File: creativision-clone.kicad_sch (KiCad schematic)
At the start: 102 parts, among them J1 Conn_01x10_Socket, J2 Conn_01x10_Socket, J3 Conn_01x07_Pin, J4 Conn_01x04_Socket, J5 RCJ-013, J6 RCJ-014, P1 Cartridge Slot, Q1 2n4401, SW1 Reset, SW2 SW_DPDT_x2, U1 AS6C62256-DIP, U100 74HCT574, U101 74HCT574, U102 74HCT574, U12 74LS32, U15 74LS139, U18 AS6C62256-DIP, U2 6502, U20 27256, U21 6821, U22 SN76489AN, U3 TMS9918A, U99 74HCT04, X1 2MHz, X2 USB-B1HSB6, Y1 10.73863MHz

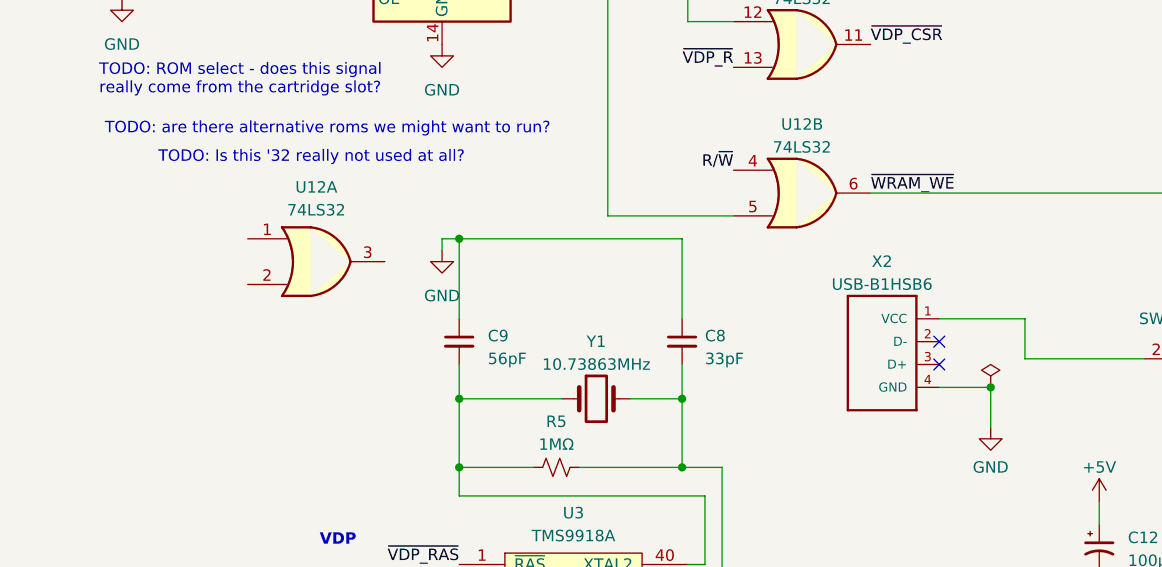
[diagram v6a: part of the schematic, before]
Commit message: Beginning footprint assignment
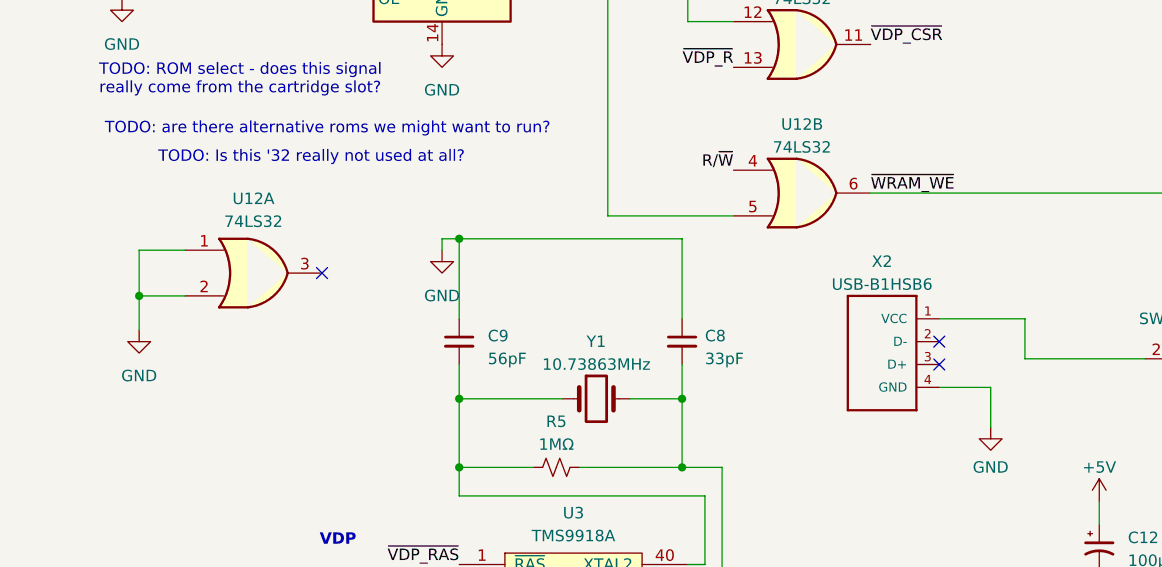
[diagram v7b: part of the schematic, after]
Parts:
- J5: footprint CUI_RCJ-017 -> Jacks:CUI_RCJ-017;  Manufacturer recommendations -> (none); Digi-Key (none) -> Manufacturer recommendations
- J6: footprint CUI_RCJ-017 -> Jacks:CUI_RCJ-017;  Manufacturer recommendations -> (none)
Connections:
- net GND: now also U12.1, U12.2
- no-connect marks 11 -> 12
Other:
- moved on the sheet: U12A
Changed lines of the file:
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@@
   (junction (at 307.975 66.675) (diameter 0) (color 0 0 0 0)
   )
+  (junction (at 18.415 204.47) (diameter 0) (color 0 0 0 0)
+  )
   (junction (at 328.93 22.86) (diameter 0) (color 0 0 0 0)
   )
@@
   (junction (at 310.515 73.025) (diameter 0) (color 0 0 0 0)
   )
-  (junction (at 113.03 214.63) (diameter 0) (color 0 0 0 0)
-  )
   (junction (at 325.755 165.735) (diameter 0) (color 0 0 0 0)
   )
@@
   (no_connect (at 79.375 239.395))
   (no_connect (at 107.315 212.09))
+  (no_connect (at 38.735 201.93))
   (no_connect (at 82.55 116.84))
   (no_connect (at 82.55 129.54))
@@
     (stroke (width 0) (type default))
   )
+  (wire (pts (xy 18.415 204.47) (xy 23.495 204.47))
+    (stroke (width 0) (type default))
+  )
   (wire (pts (xy 331.47 52.705) (xy 331.47 69.215))
     (stroke (width 0) (type default))
@@
     (stroke (width 0) (type default))
   )
+  (wire (pts (xy 18.415 199.39) (xy 23.495 199.39))
+    (stroke (width 0) (type default))
+  )
   (wire (pts (xy 319.405 88.265) (xy 302.895 88.265))
     (stroke (width 0) (type default))
@@
     (stroke (width 0) (type default))
   )
+  (wire (pts (xy 18.415 208.28) (xy 18.415 204.47))
+    (stroke (width 0) (type default))
+  )
   (wire (pts (xy 276.86 233.045) (xy 276.86 229.235))
     (stroke (width 0) (type default))
@@
     (stroke (width 0) (type default))
   )
+  (wire (pts (xy 18.415 204.47) (xy 18.415 199.39))
+    (stroke (width 0) (type default))
+  )
   (wire (pts (xy 129.54 57.15) (xy 141.605 57.15))
     (stroke (width 0) (type default))
@@
     )
   )
-  (symbol (lib_id "power:PWR_FLAG") (at 113.03 214.63 0) (unit 1)
-    (in_bom yes) (on_board yes) (dnp no) (fields_autoplaced)
-    (property "Reference" "#FLG05" (at 113.03 212.725 0)
-      (effects (font (size 1.27 1.27)) hide)
-    )
-    (property "Value" "PWR_FLAG" (at 113.03 210.82 0)
-      (effects (font (size 1.27 1.27)) hide)
-    )
-    (property "Footprint" "" (at 113.03 214.63 0)
-      (effects (font (size 1.27 1.27)) hide)
-    )
-    (property "Datasheet" "~" (at 113.03 214.63 0)
-      (effects (font (size 1.27 1.27)) hide)
-    )
-    (pin "1")
-    (instances
-      (project "creativision-clone"
-        (path "/4f154aad-bddd-4366-bec7-a527fffe24b1"
-          (reference "#FLG05") (unit 1)
-        )
-      )
-    )
-  )
   (symbol (lib_id "power:+9V") (at 153.67 233.68 0) (unit 1)
     (in_bom yes) (on_board yes) (dnp no) (fields_autoplaced)
@@
     )
   )
+  (symbol (lib_id "power:GND") (at 18.415 208.28 0) (unit 1)
+    (in_bom yes) (on_board yes) (dnp no) (fields_autoplaced)
+    (property "Reference" "#PWR070" (at 18.415 214.63 0)
+      (effects (font (size 1.27 1.27)) hide)
+    )
+    (property "Value" "GND" (at 18.415 213.36 0)
+      (effects (font (size 1.27 1.27)))
+    )
+    (property "Footprint" "" (at 18.415 208.28 0)
+      (effects (font (size 1.27 1.27)) hide)
+    )
+    (property "Datasheet" "" (at 18.415 208.28 0)
+      (effects (font (size 1.27 1.27)) hide)
+    )
+    (pin "1")
+    (instances
+      (project "creativision-clone"
+        (path "/4f154aad-bddd-4366-bec7-a527fffe24b1"
+          (reference "#PWR070") (unit 1)
+        )
+      )
+    )
+  )
   (symbol (lib_id "power:GND") (at 158.75 299.085 0) (unit 1)
     (in_bom yes) (on_board yes) (dnp no) (fields_autoplaced)
@@
       (effects (font (size 1.27 1.27)) (justify right))
     )
-    (property "Footprint" "CUI_RCJ-017" (at 383.54 187.325 0)
+    (property "Footprint" "Jacks:CUI_RCJ-017" (at 383.54 187.325 0)
       (effects (font (size 1.27 1.27)) (justify left bottom) hide)
     )
@@
       (effects (font (size 1.27 1.27)) (justify left bottom) hide)
     )
-    (property "" "Manufacturer recommendations" (at 383.54 187.325 0)
+    (property "Digi-Key" "Manufacturer recommendations" (at 383.54 187.325 0)
       (effects (font (size 1.27 1.27)) (justify left bottom) hide)
     )
@@
       (effects (font (size 1.27 1.27)))
     )
-    (property "Footprint" "CUI_RCJ-017" (at 383.54 168.275 0)
+    (property "Footprint" "Jacks:CUI_RCJ-017" (at 383.54 168.275 0)
       (effects (font (size 1.27 1.27)) (justify left bottom) hide)
     )
@@
       (effects (font (size 1.27 1.27)) (justify left bottom) hide)
     )
-    (property "" "Manufacturer recommendations" (at 383.54 168.275 0)
+    (property "Digi-Key" "" (at 383.54 168.275 0)
       (effects (font (size 1.27 1.27)) (justify left bottom) hide)
     )
+    (property "Field5" "" (at 383.54 168.275 0)
+      (effects (font (size 1.27 1.27)) hide)
+    )
     (pin "1A")
     (pin "1B")
@@
     )
   )
-  (symbol (lib_id "74xx:74LS32") (at 38.1 200.66 0) (unit 1)
+  (symbol (lib_id "74xx:74LS32") (at 31.115 201.93 0) (unit 1)
     (in_bom yes) (on_board yes) (dnp no) (fields_autoplaced)
-    (property "Reference" "U12" (at 38.1 192.405 0)
+    (property "Reference" "U12" (at 31.115 193.675 0)
       (effects (font (size 1.27 1.27)))
     )
-    (property "Value" "74LS32" (at 38.1 194.945 0)
+    (property "Value" "74LS32" (at 31.115 196.215 0)
       (effects (font (size 1.27 1.27)))
     )
-    (property "Footprint" "" (at 38.1 200.66 0)
+    (property "Footprint" "" (at 31.115 201.93 0)
       (effects (font (size 1.27 1.27)) hide)
     )
-    (property "Datasheet" "http://www.ti.com/lit/gpn/sn74LS32" (at 38.1 200.66 0)
+    (property "Datasheet" "http://www.ti.com/lit/gpn/sn74LS32" (at 31.115 201.93 0)
       (effects (font (size 1.27 1.27)) hide)
     )

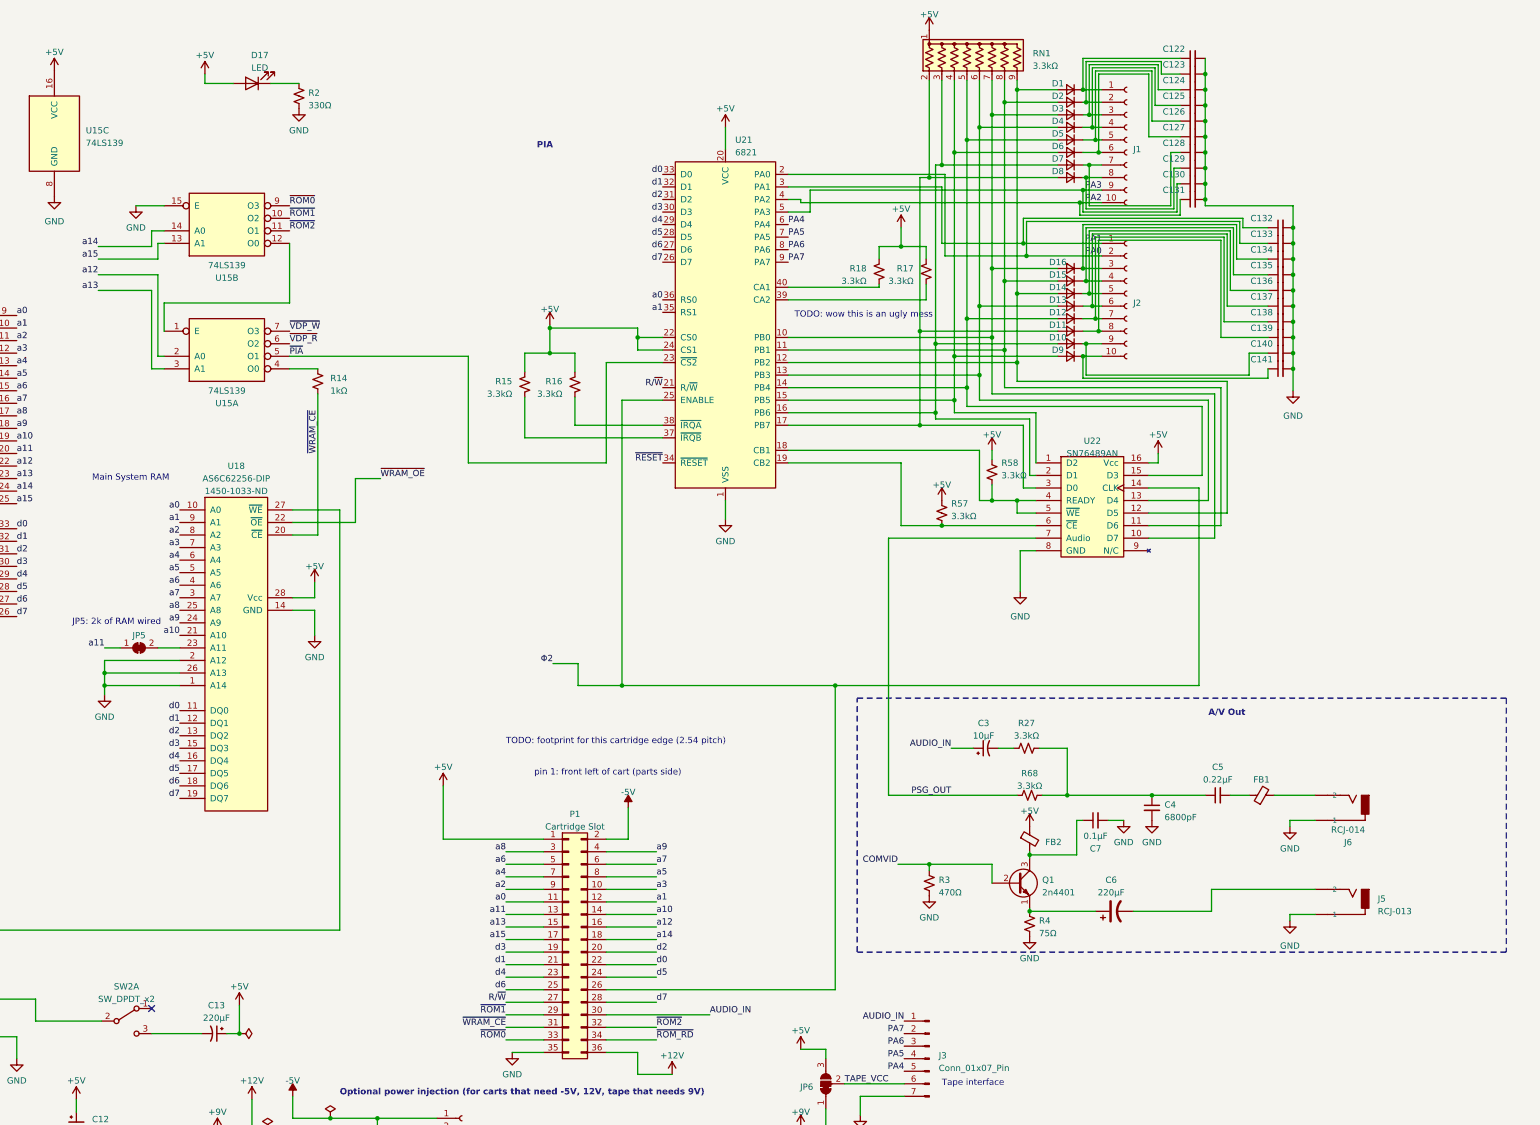
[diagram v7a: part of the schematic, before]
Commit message: Almost complete footprint assignment
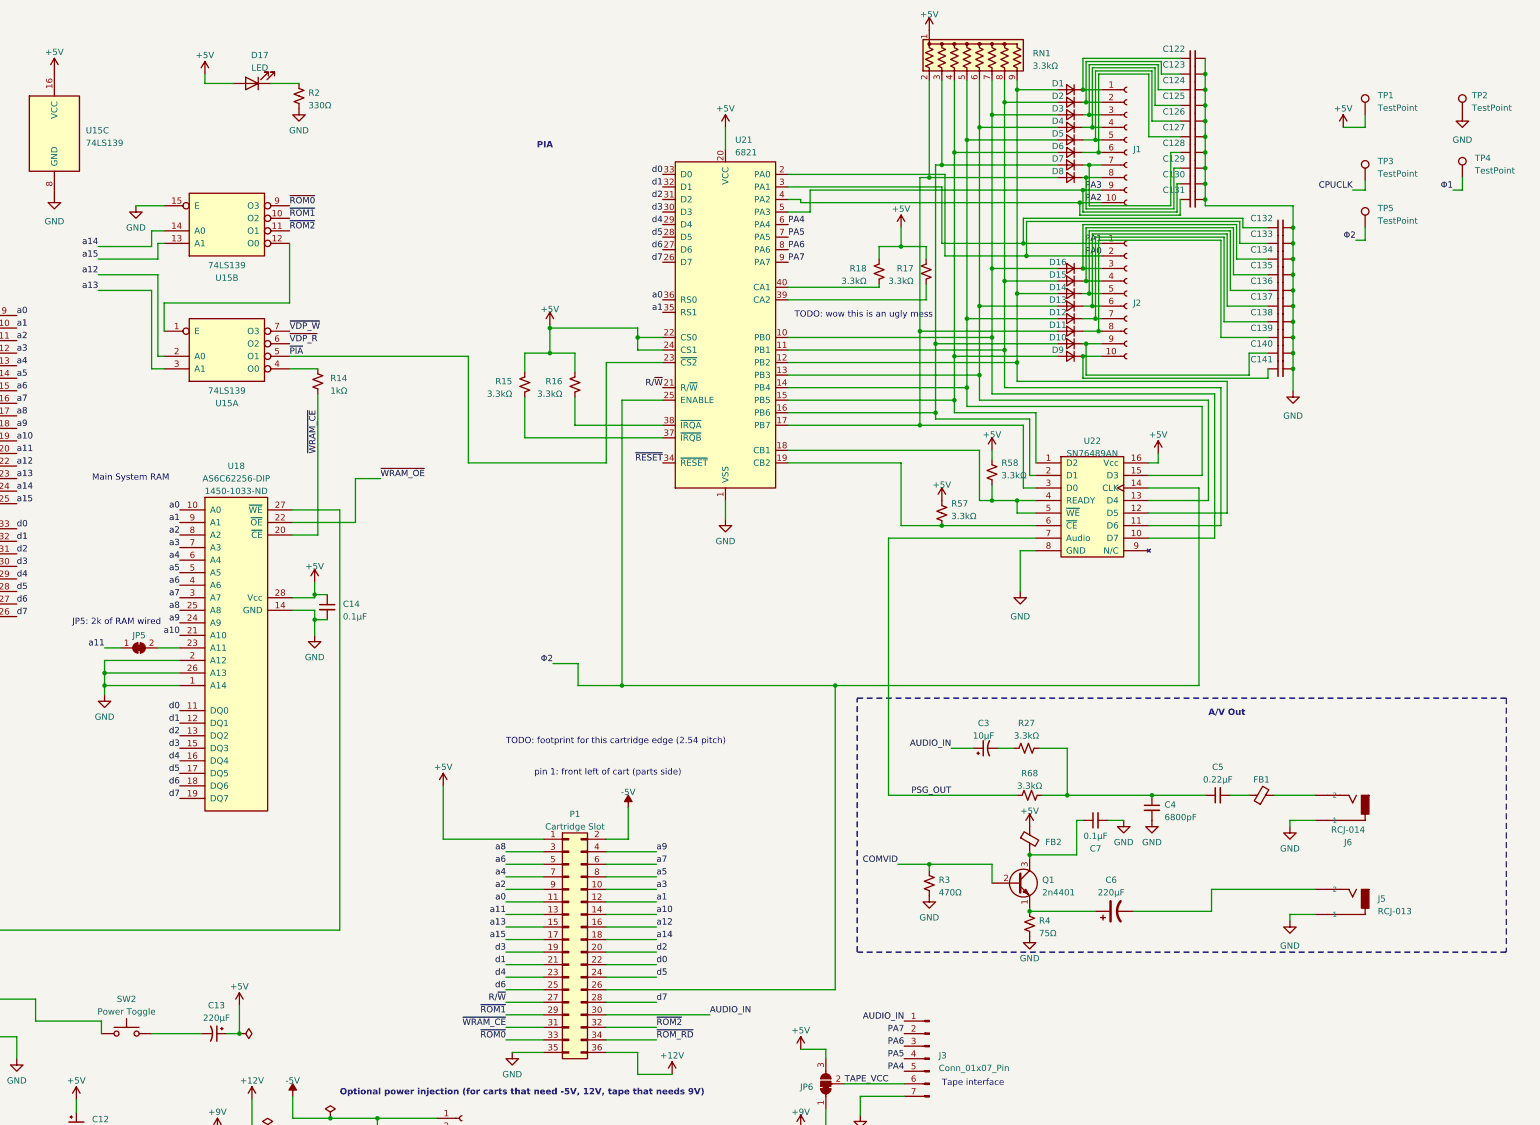
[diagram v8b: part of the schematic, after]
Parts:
- removed SW2: SW_DPDT_x2, symbol Switch:SW_DPDT_x2
- added C14: 0.1µF, Capacitor_THT:C_Disc_D5.0mm_W2.5mm_P2.50mm, symbol Device:C_Small
- added SW2: Power Toggle, LeakyChips:PVA1_Switch, symbol Switch:SW_Push
- added TP1, TP2, TP3, TP4, TP5: TestPoint, TestPoint:TestPoint_Loop_D2.50mm_Drill1.0mm, symbol Connector:TestPoint
- C1, C122, C123, C124, C125, C126, C127, C128, C129, C130, C131, C132, C133, C134, C135, C136, C137, C138, C139, C140, C141, C2, C4, C5, C7, C8, C9: footprint (none) -> Capacitor_THT:C_Disc_D5.0mm_W2.5mm_P2.50mm
- C10, C106, C11, C12, C13, C6: footprint (none) -> Capacitor_THT:CP_Radial_D6.3mm_P2.50mm
- C3: footprint (none) -> Capacitor_THT:CP_Radial_D5.0mm_P2.50mm
- D1, D10, D11, D12, D13, D14, D15, D16, D2, D3, D4, D5, D6, D7, D8, D9: footprint (none) -> Diode_THT:D_DO-35_SOD27_P7.62mm_Horizontal
- D17: footprint (none) -> LED_THT:LED_D3.0mm
- FB1, FB2: footprint (none) -> Resistor_THT:R_Axial_DIN0309_L9.0mm_D3.2mm_P12.70mm_Horizontal; DigiKey (none) -> 1934-1476-2-ND
- J1, J2: footprint (none) -> Connector_PinSocket_2.54mm:PinSocket_1x10_P2.54mm_Vertical
- J3: footprint (none) -> Connector_PinHeader_2.54mm:PinHeader_1x07_P2.54mm_Horizontal
- J4: footprint (none) -> Connector_PinSocket_2.54mm:PinSocket_1x04_P2.54mm_Vertical
- JP1, JP2, JP3, JP4, JP5: footprint (none) -> Jumper:SolderJumper-2_P1.3mm_Bridged2Bar_RoundedPad1.0x1.5mm
- JP6: footprint (none) -> Jumper:SolderJumper-3_P1.3mm_Bridged12_RoundedPad1.0x1.5mm_NumberLabels
- Q1: footprint (none) -> Package_TO_SOT_THT:TO-92_Inline_Wide
- R1, R10, R14, R15, R16, R17, R18, R2, R27, R3, R4, R5, R57, R58, R66, R68: footprint (none) -> Resistor_THT:R_Axial_DIN0207_L6.3mm_D2.5mm_P10.16mm_Horizontal
- SW1: footprint (none) -> Button_Switch_THT:SW_PUSH_6mm
- U1, U18: footprint Housings_DIP:DIP-28_W15.24mm_Socket_LongPads -> Package_DIP:DIP-28_W15.24mm_Socket_LongPads
- U100, U101, U102: footprint (none) -> Package_DIP:DIP-20_W7.62mm_Socket_LongPads
- U12, U99: footprint (none) -> Package_DIP:DIP-14_W7.62mm_Socket_LongPads
- U15, U22: footprint (none) -> Package_DIP:DIP-16_W7.62mm_Socket_LongPads
- U3: footprint Housings_DIP:DIP-40_W15.24mm_Socket_LongPads -> Package_DIP:DIP-40_W25.4mm_Socket_LongPads
- X2: footprint OST_USB-B1HSB6 -> USB-B1HSB6:OST_USB-B1HSB6
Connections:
- net +5V: now also C14.1, TP1.1
- net CPUCLK: now also TP3.1
- net GND: now also C14.2, TP2.1
- net Φ1: now also TP4.1
- net Φ2: now also TP5.1
- net at C13.2: now also SW2.2
- net at X2.1 (VCC): now also SW2.1
- no-connect marks 12 -> 11
